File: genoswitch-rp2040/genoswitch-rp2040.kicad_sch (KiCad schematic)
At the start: 35 parts, among them J1 USB_B_Micro, J2 Conn_01x03_Socket-PicoDebug, SW1 PTS815_SJM_250_SMTR_LFS, U1 NCP1117-3.3_SOT223, U2 W25Q128JVS, U3 RP2040, U4 MCP1501-10xCH, U5_HW-SPI0 MCP3008, U6_HW-SPI1 MCP3008, U7_PIO-SPI0 MCP3008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

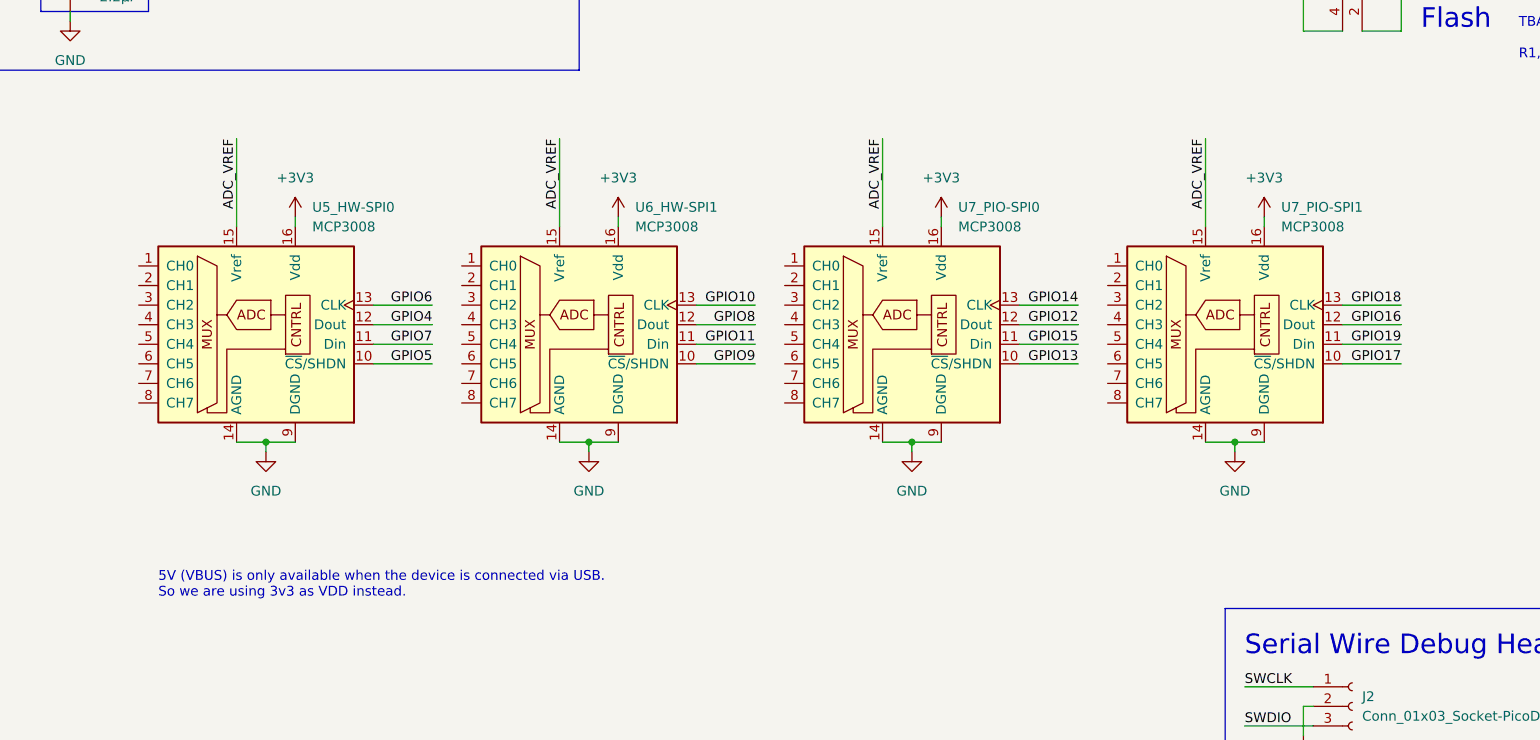
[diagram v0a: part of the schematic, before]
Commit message: Remove MCP3008s from main PCB, add connectors instead
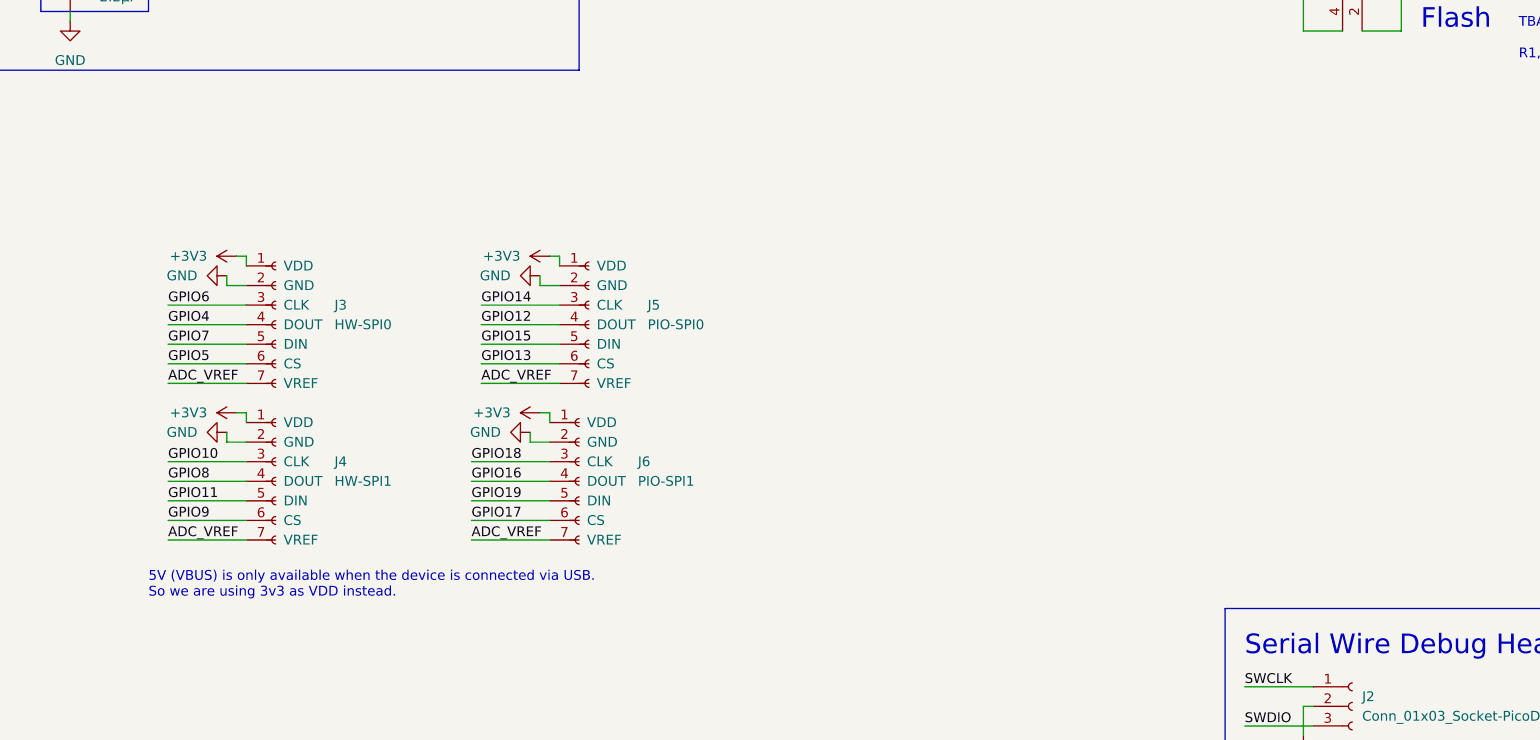
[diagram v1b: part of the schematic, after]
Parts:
- removed U5_HW-SPI0, U6_HW-SPI1, U7_PIO-SPI0, U7_PIO-SPI1: MCP3008, Package_SO:SOIC-16_3.9x9.9mm_P1.27mm, symbol Analog_ADC:MCP3008
- added J3: HW-SPI0, Connector_JST:JST_PH_B7B-PH-K_1x07_P2.00mm_Vertical, symbol Genoswitch_Custom:GS_ADC_Socket
- added J4: HW-SPI1, Connector_JST:JST_PH_B7B-PH-K_1x07_P2.00mm_Vertical, symbol Genoswitch_Custom:GS_ADC_Socket
- added J5: PIO-SPI0, Connector_JST:JST_PH_B7B-PH-K_1x07_P2.00mm_Vertical, symbol Genoswitch_Custom:GS_ADC_Socket
- added J6: PIO-SPI1, Connector_JST:JST_PH_B7B-PH-K_1x07_P2.00mm_Vertical, symbol Genoswitch_Custom:GS_ADC_Socket
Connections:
- net +3V3: now also J3.1 (VDD), J4.1 (VDD), J5.1 (VDD), J6.1 (VDD)
- net ADC_VREF: now also J3.7 (VREF), J4.7 (VREF), J5.7 (VREF), J6.7 (VREF)
- net GND: now also J3.2 (GND), J4.2 (GND), J5.2 (GND), J6.2 (GND)
- net GPIO10: now also J4.3 (CLK)
- net GPIO11: now also J4.5 (DIN)
- net GPIO12: now also J5.4 (DOUT)
- net GPIO13: now also J5.6 (CS)
- net GPIO14: now also J5.3 (CLK)
- net GPIO15: now also J5.5 (DIN)
- net GPIO16: now also J6.4 (DOUT)
- net GPIO17: now also J6.6 (CS)
- net GPIO18: now also J6.3 (CLK)
- net GPIO19: now also J6.5 (DIN)
- net GPIO4: now also J3.4 (DOUT)
- net GPIO5: now also J3.6 (CS)
- net GPIO6: now also J3.3 (CLK)
- net GPIO7: now also J3.5 (DIN)
- net GPIO8: now also J4.4 (DOUT)
- net GPIO9: now also J4.6 (CS)

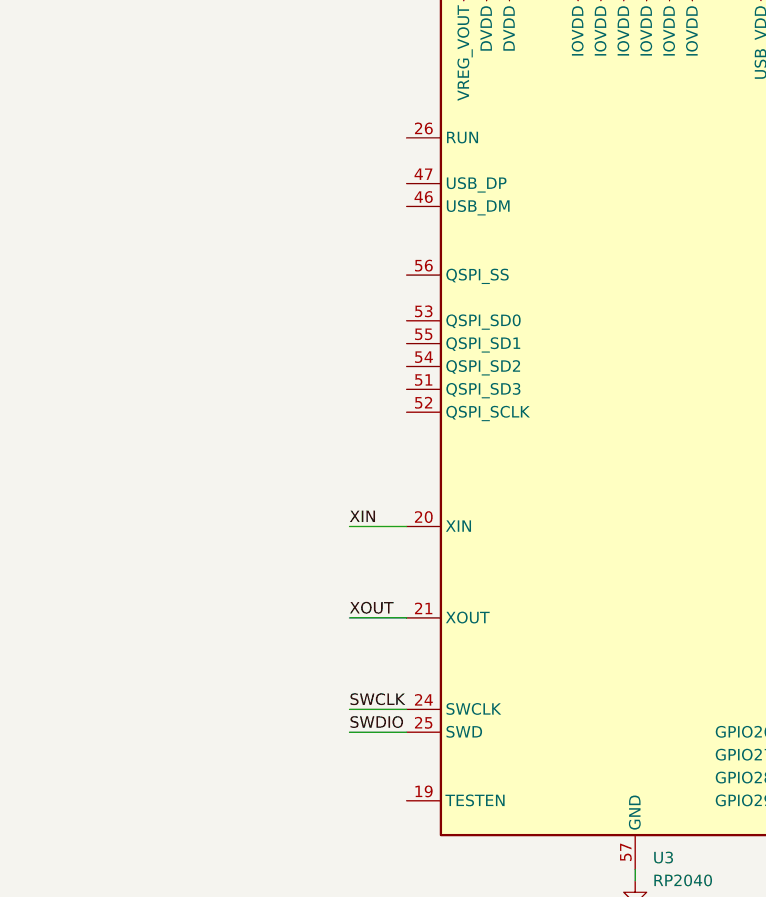
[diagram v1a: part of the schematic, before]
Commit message: Add missing connections to RP2040 SoC
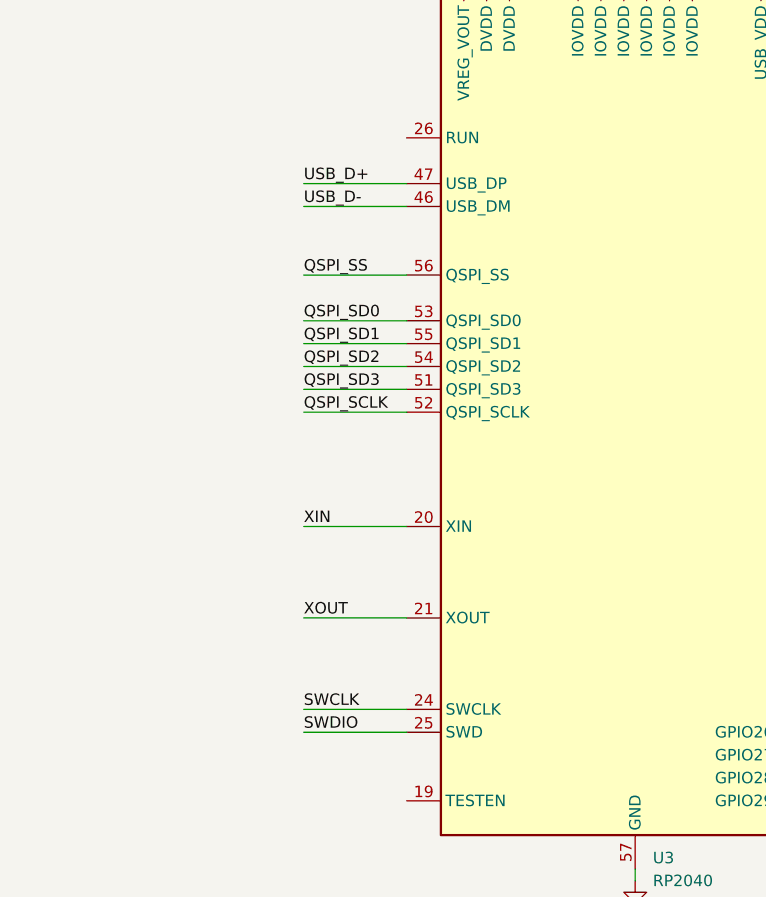
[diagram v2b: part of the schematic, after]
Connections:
- net QSPI_SCLK: now also U3.52 (QSPI_SCLK)
- net QSPI_SD0: now also U3.53 (QSPI_SD0)
- net QSPI_SD1: now also U3.55 (QSPI_SD1)
- net QSPI_SD2: now also U3.54 (QSPI_SD2)
- net QSPI_SD3: now also U3.51 (QSPI_SD3)
- net QSPI_SS: now also U3.56 (QSPI_SS)
- net USB_D+: now also U3.47 (USB_DP)
- net USB_D-: now also U3.46 (USB_DM)
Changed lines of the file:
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@@
     (stroke (width 0) (type default))
   )
-  (wire (pts (xy 49.53 121.92) (xy 55.88 121.92))
+  (wire (pts (xy 44.45 121.92) (xy 55.88 121.92))
     (stroke (width 0) (type default))
   )
@@
     (stroke (width 0) (type default))
   )
-  (wire (pts (xy 49.53 132.08) (xy 55.88 132.08))
+  (wire (pts (xy 44.45 132.08) (xy 55.88 132.08))
     (stroke (width 0) (type default))
   )
@@
     (stroke (width 0) (type default))
   )
-  (wire (pts (xy 49.53 111.76) (xy 55.88 111.76))
+  (wire (pts (xy 44.45 111.76) (xy 55.88 111.76))
     (stroke (width 0) (type default))
   )
@@
     (stroke (width 0) (type default))
   )
+  (wire (pts (xy 44.45 83.82) (xy 55.88 83.82))
+    (stroke (width 0) (type default))
+  )
   (wire (pts (xy 107.95 22.86) (xy 95.25 22.86))
     (stroke (width 0) (type default))
@@
     (stroke (width 0) (type default))
   )
+  (wire (pts (xy 55.88 88.9) (xy 44.45 88.9))
+    (stroke (width 0) (type default))
+  )
   (wire (pts (xy 137.16 33.02) (xy 133.35 33.02))
     (stroke (width 0) (type default))
@@
     (stroke (width 0) (type default))
   )
+  (wire (pts (xy 55.88 96.52) (xy 44.45 96.52))
+    (stroke (width 0) (type default))
+  )
   (wire (pts (xy 107.95 22.86) (xy 107.95 24.13))
     (stroke (width 0) (type default))
@@
     (stroke (width 0) (type default))
   )
-  (wire (pts (xy 49.53 134.62) (xy 55.88 134.62))
+  (wire (pts (xy 44.45 134.62) (xy 55.88 134.62))
     (stroke (width 0) (type default))
   )
@@
     (stroke (width 0) (type default))
   )
+  (wire (pts (xy 55.88 93.98) (xy 44.45 93.98))
+    (stroke (width 0) (type default))
+  )
   (wire (pts (xy 106.68 96.52) (xy 121.92 96.52))
     (stroke (width 0) (type default))
@@
     (stroke (width 0) (type default))
   )
+  (wire (pts (xy 55.88 99.06) (xy 44.45 99.06))
+    (stroke (width 0) (type default))
+  )
   (wire (pts (xy 120.65 33.02) (xy 107.95 33.02))
     (stroke (width 0) (type default))
@@
     (stroke (width 0) (type default))
   )
+  (wire (pts (xy 55.88 91.44) (xy 44.45 91.44))
+    (stroke (width 0) (type default))
+  )
+  (wire (pts (xy 44.45 76.2) (xy 55.88 76.2))
+    (stroke (width 0) (type default))
+  )
   (wire (pts (xy 106.68 53.34) (xy 106.68 54.61))
     (stroke (width 0) (type default))
@@
   )
   (wire (pts (xy 106.68 83.82) (xy 121.92 83.82))
+    (stroke (width 0) (type default))
+  )
+  (wire (pts (xy 44.45 73.66) (xy 55.88 73.66))
     (stroke (width 0) (type default))
   )
@@
     (effects (font (size 1.27 1.27)) (justify right bottom))
   )
-  (label "XIN" (at 49.53 111.76 0) (fields_autoplaced)
+  (label "XIN" (at 44.45 111.76 0) (fields_autoplaced)
     (effects (font (size 1.27 1.27)) (justify left bottom))
   )
@@
     (effects (font (size 1.27 1.27)) (justify right bottom))
   )
+  (label "QSPI_SD1" (at 44.45 91.44 0) (fields_autoplaced)
+    (effects (font (size 1.27 1.27)) (justify left bottom))
+  )
   (label "QSPI_SD0" (at 381 52.07 90) (fields_autoplaced)
     (effects (font (size 1.27 1.27)) (justify left bottom))
   )
-  (label "SWDIO" (at 49.53 134.62 0) (fields_autoplaced)
+  (label "SWDIO" (at 44.45 134.62 0) (fields_autoplaced)
     (effects (font (size 1.27 1.27)) (justify left bottom))
   )
@@
     (effects (font (size 1.27 1.27)) (justify right bottom))
   )
-  (label "XOUT" (at 49.53 121.92 0) (fields_autoplaced)
+  (label "XOUT" (at 44.45 121.92 0) (fields_autoplaced)
     (effects (font (size 1.27 1.27)) (justify left bottom))
   )
@@
     (effects (font (size 1.27 1.27)) (justify right bottom))
   )
+  (label "QSPI_SD0" (at 44.45 88.9 0) (fields_autoplaced)
+    (effects (font (size 1.27 1.27)) (justify left bottom))
+  )
   (label "GPIO13" (at 223.52 95.25 0) (fields_autoplaced)
     (effects (font (size 1.27 1.27)) (justify left bottom))
@@
     (effects (font (size 1.27 1.27)) (justify left bottom))
   )
+  (label "QSPI_SCLK" (at 44.45 99.06 0) (fields_autoplaced)
+    (effects (font (size 1.27 1.27)) (justify left bottom))
+  )
   (label "GPIO9" (at 121.92 88.9 180) (fields_autoplaced)
     (effects (font (size 1.27 1.27)) (justify right bottom))
@@
     (effects (font (size 1.27 1.27)) (justify right bottom))
   )
-  (label "SWCLK" (at 49.53 132.08 0) (fields_autoplaced)
+  (label "SWCLK" (at 44.45 132.08 0) (fields_autoplaced)
     (effects (font (size 1.27 1.27)) (justify left bottom))
   )
@@
     (effects (font (size 1.27 1.27)) (justify left bottom))
   )
+  (label "QSPI_SD2" (at 44.45 93.98 0) (fields_autoplaced)
+    (effects (font (size 1.27 1.27)) (justify left bottom))
+  )
   (label "XOUT" (at 361.95 176.53 180) (fields_autoplaced)
     (effects (font (size 1.27 1.27)) (justify right bottom))
@@
     (effects (font (size 1.27 1.27)) (justify right bottom))
   )
+  (label "QSPI_SS" (at 44.45 83.82 0) (fields_autoplaced)
+    (effects (font (size 1.27 1.27)) (justify left bottom))
+  )
   (label "GPIO13" (at 121.92 99.06 180) (fields_autoplaced)
     (effects (font (size 1.27 1.27)) (justify right bottom))
@@
     (effects (font (size 1.27 1.27)) (justify left bottom))
   )
+  (label "USB_D+" (at 44.45 73.66 0) (fields_autoplaced)
+    (effects (font (size 1.27 1.27)) (justify left bottom))
+  )
   (label "GPIO17" (at 222.25 115.57 0) (fields_autoplaced)
     (effects (font (size 1.27 1.27)) (justify left bottom))
@@
     (effects (font (size 1.27 1.27)) (justify left bottom))
   )
+  (label "QSPI_SD3" (at 44.45 96.52 0) (fields_autoplaced)
+    (effects (font (size 1.27 1.27)) (justify left bottom))
+  )
   (label "GPIO15" (at 223.52 92.71 0) (fields_autoplaced)
     (effects (font (size 1.27 1.27)) (justify left bottom))
@@
     (effects (font (size 1.27 1.27)) (justify right bottom))
   )
+  (label "USB_D-" (at 44.45 76.2 0) (fields_autoplaced)
+    (effects (font (size 1.27 1.27)) (justify left bottom))
+  )
   (label "GPIO4" (at 121.92 76.2 180) (fields_autoplaced)

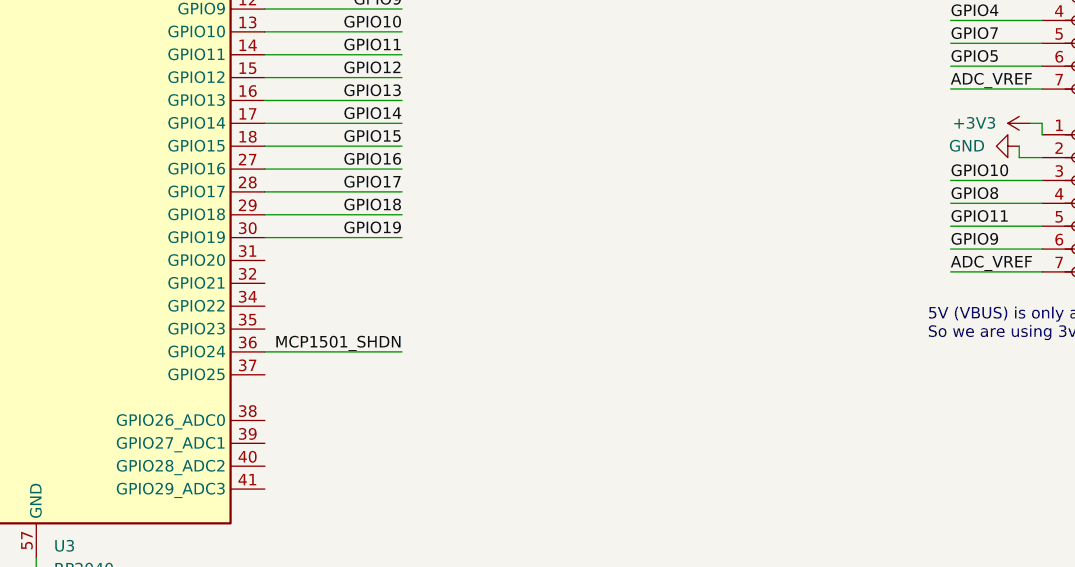
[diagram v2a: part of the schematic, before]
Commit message: Add device detection pin connections
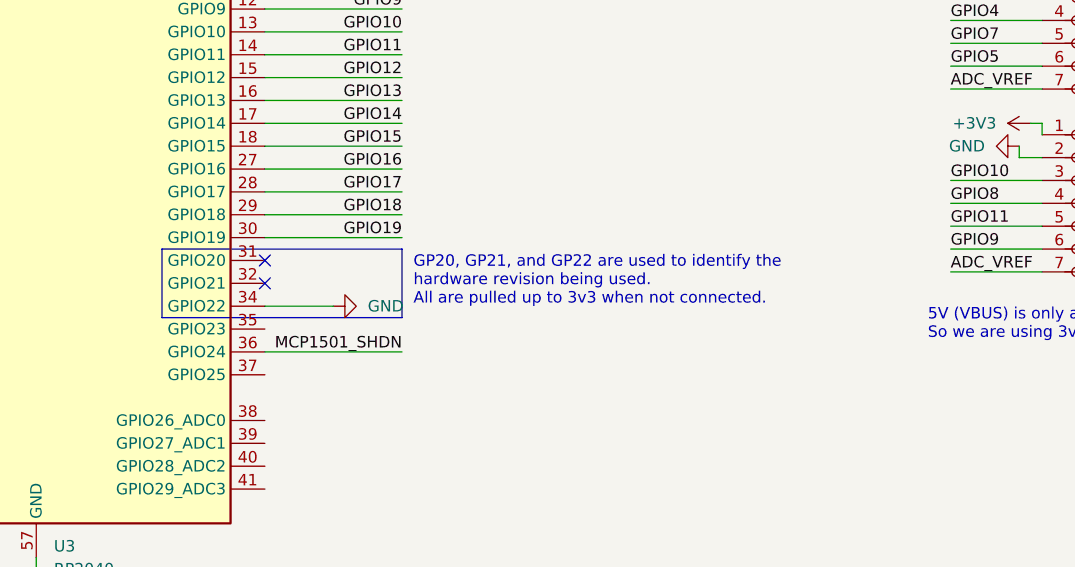
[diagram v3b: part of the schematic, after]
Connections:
- net GND: now also U3.34 (GPIO22)
- no-connect marks 1 -> 3
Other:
- note added: "GP20, GP21, and GP22 are used to identify the hardware revision being used. All are pulled up to 3v3 when not connected."
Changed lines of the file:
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@@
   )
   (no_connect (at 314.96 232.41))
+  (no_connect (at 106.68 119.38))
+  (no_connect (at 106.68 116.84))
   (wire (pts (xy 106.68 101.6) (xy 121.92 101.6))
     (stroke (width 0) (type default))
@@
   )
   (wire (pts (xy 361.95 26.67) (xy 363.22 26.67))
+    (stroke (width 0) (type default))
+  )
+  (wire (pts (xy 106.68 121.92) (xy 114.3 121.92))
     (stroke (width 0) (type default))
   )
@@
     (fill (type none))
   )
+  (rectangle (start 95.25 115.57) (end 121.92 123.19)
+    (stroke (width 0) (type default) (color 255 0 255 1))
+    (fill (type none))
+  )
   (rectangle (start 34.29 24.13) (end 143.51 31.75)
     (stroke (width 0) (type default) (color 255 153 0 1))
@@
     (at 72.39 38.1 0)
     (effects (font (size 1.27 1.27) (color 255 153 0 1)) (justify left bottom))
+  )
+  (text "GP20, GP21, and GP22 are used to identify the\nhardware revision being used.\nAll are pulled up to 3v3 when not connected."
+    (at 123.19 121.92 0)
+    (effects (font (size 1.27 1.27) (color 255 0 255 1)) (justify left bottom))
   )
   (text "Power" (at 336.55 208.28 0)
@@
         )
       )
+    )
+  )
+  (symbol (lib_id "power:GND") (at 114.3 121.92 90) (unit 1)
+    (in_bom yes) (on_board yes) (dnp no) (fields_autoplaced)
+    (property "Reference" "#PWR030" (at 120.65 121.92 0)
+      (effects (font (size 1.27 1.27)) hide)
+    )
+    (property "Value" "GND" (at 118.11 121.92 90)
+      (effects (font (size 1.27 1.27)) (justify right))
+    )
+    (property "Footprint" "" (at 114.3 121.92 0)
+      (effects (font (size 1.27 1.27)) hide)
+    )
+    (property "Datasheet" "" (at 114.3 121.92 0)
+      (effects (font (size 1.27 1.27)) hide)
+    )
+    (pin "1")
+    (instances
+      (project "genoswitch-rp2040"
+        (path "/2e7ee4d9-1204-4a0f-bb2c-fb0f0d4af2cf"
+          (reference "#PWR030") (unit 1)
+        )
+      )
